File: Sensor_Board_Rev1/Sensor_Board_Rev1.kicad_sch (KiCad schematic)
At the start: 0 parts

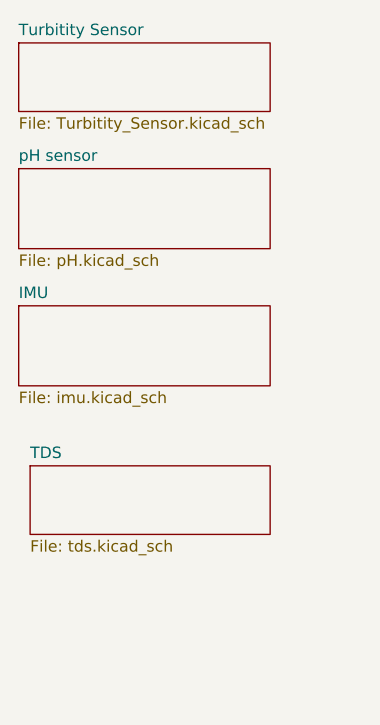
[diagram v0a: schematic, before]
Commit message: Changing MPU6050 chip to MPU9250 breakout
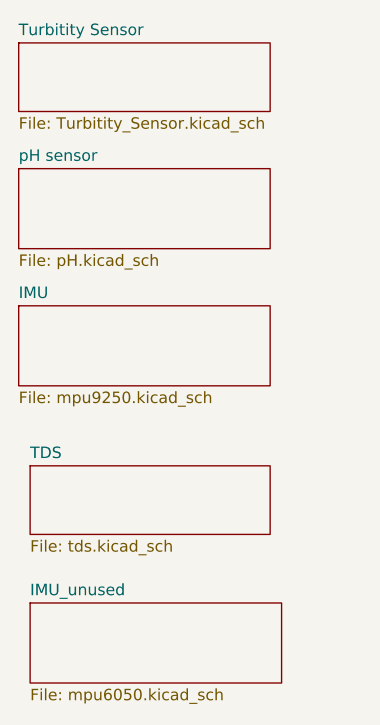
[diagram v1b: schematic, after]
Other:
- added sheet IMU_unused (mpu6050.kicad_sch)
- sheet IMU: file imu.kicad_sch -> mpu9250.kicad_sch
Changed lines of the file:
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@@
 (kicad_sch
-	(version 20250114)
+	(version 20260306)
 	(generator "eeschema")
-	(generator_version "9.0")
+	(generator_version "10.0")
 	(paper "A4")
+	(sheet
+		(at 34.29 111.76)
+		(size 27.94 8.89)
+		(exclude_from_sim no)
+		(in_bom yes)
+		(on_board yes)
+		(dnp no)
+		(fields_autoplaced yes)
+		(stroke
+			(width 0.1524)
+			(type solid)
+		)
+		(fill
+			(color 0 0 0 0)
+		)
+		(property "Sheetname" "IMU_unused"
+			(at 34.29 111.0484 0)
+			(show_name no)
+			(do_not_autoplace no)
+			(effects
+				(font
+					(size 1.27 1.27)
+				)
+				(justify left bottom)
+			)
+		)
+		(property "Sheetfile" "mpu6050.kicad_sch"
+			(at 34.29 121.2346 0)
+			(show_name no)
+			(do_not_autoplace no)
+			(effects
+				(font
+					(size 1.27 1.27)
+				)
+				(justify left top)
+			)
+		)
+		(instances
+			(project "Sensor_Board_Rev1"
+				(path "/757ff33a-3003-4f35-ac3f-a6ccfb0c40fd"
+					(page "6")
+				)
+			)
+		)
+	)
 	(sheet
 		(at 33.02 63.5)
@@
 		)
 		(fill
-			(color 0 0 0 0.0000)
+			(color 0 0 0 0)
 		)
 		(property "Sheetname" "pH sensor"
 			(at 33.02 62.7884 0)
+			(show_name no)
+			(do_not_autoplace no)
 			(effects
 				(font
@@
 		(property "Sheetfile" "pH.kicad_sch"
 			(at 33.02 72.9746 0)
+			(show_name no)
+			(do_not_autoplace no)
 			(effects
 				(font
@@
 		)
 		(fill
-			(color 0 0 0 0.0000)
+			(color 0 0 0 0)
 		)
 		(property "Sheetname" "Turbitity Sensor"
 			(at 33.02 48.8184 0)
+			(show_name no)
+			(do_not_autoplace no)
 			(effects
 				(font
@@
 		(property "Sheetfile" "Turbitity_Sensor.kicad_sch"
 			(at 33.02 57.7346 0)
+			(show_name no)
+			(do_not_autoplace no)
 			(effects
 				(font
@@
 		)
 		(fill
-			(color 0 0 0 0.0000)
+			(color 0 0 0 0)
 		)
 		(property "Sheetname" "IMU"
 			(at 33.02 78.0284 0)
-			(effects
-				(font
-					(size 1.27 1.27)
-				)
-				(justify left bottom)
-			)
-		)
-		(property "Sheetfile" "imu.kicad_sch"
+			(show_name no)
+			(do_not_autoplace no)
+			(effects
+				(font
+					(size 1.27 1.27)
+				)
+				(justify left bottom)
+			)
+		)
+		(property "Sheetfile" "mpu9250.kicad_sch"
 			(at 33.02 88.2146 0)
+			(show_name no)
+			(do_not_autoplace no)
 			(effects
 				(font
@@
 		)
 		(fill
-			(color 0 0 0 0.0000)
+			(color 0 0 0 0)
 		)
 		(property "Sheetname" "TDS"
 			(at 34.29 95.8084 0)
+			(show_name no)
+			(do_not_autoplace no)
 			(effects
 				(font
@@
 		(property "Sheetfile" "tds.kicad_sch"
 			(at 34.29 104.7246 0)
-			(effects
-				(font
+			(show_name no)
+			(do_not_autoplace no)
+			(effects
+				(font
